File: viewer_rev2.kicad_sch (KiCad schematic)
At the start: 19 parts, among them J1 USB_C_Receptacle_PowerOnly_6P, Q1 DMG3414U, SW1 SW_SPDT, U1 TLC555xD

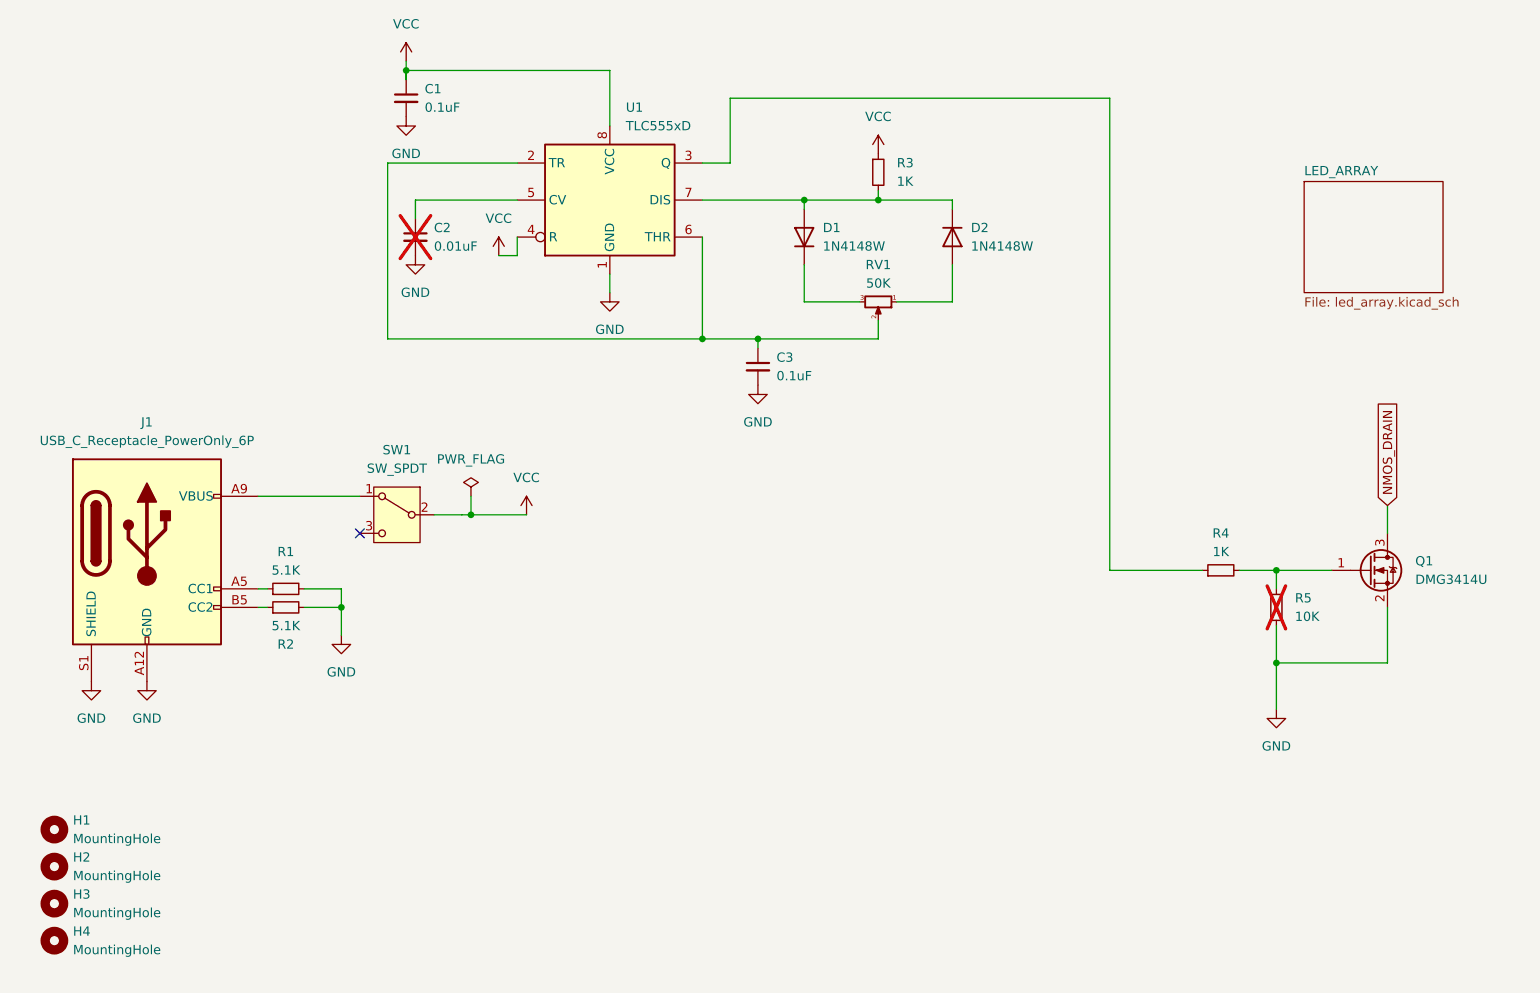
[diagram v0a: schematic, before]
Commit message: update USB-C conn and add JLC PNs
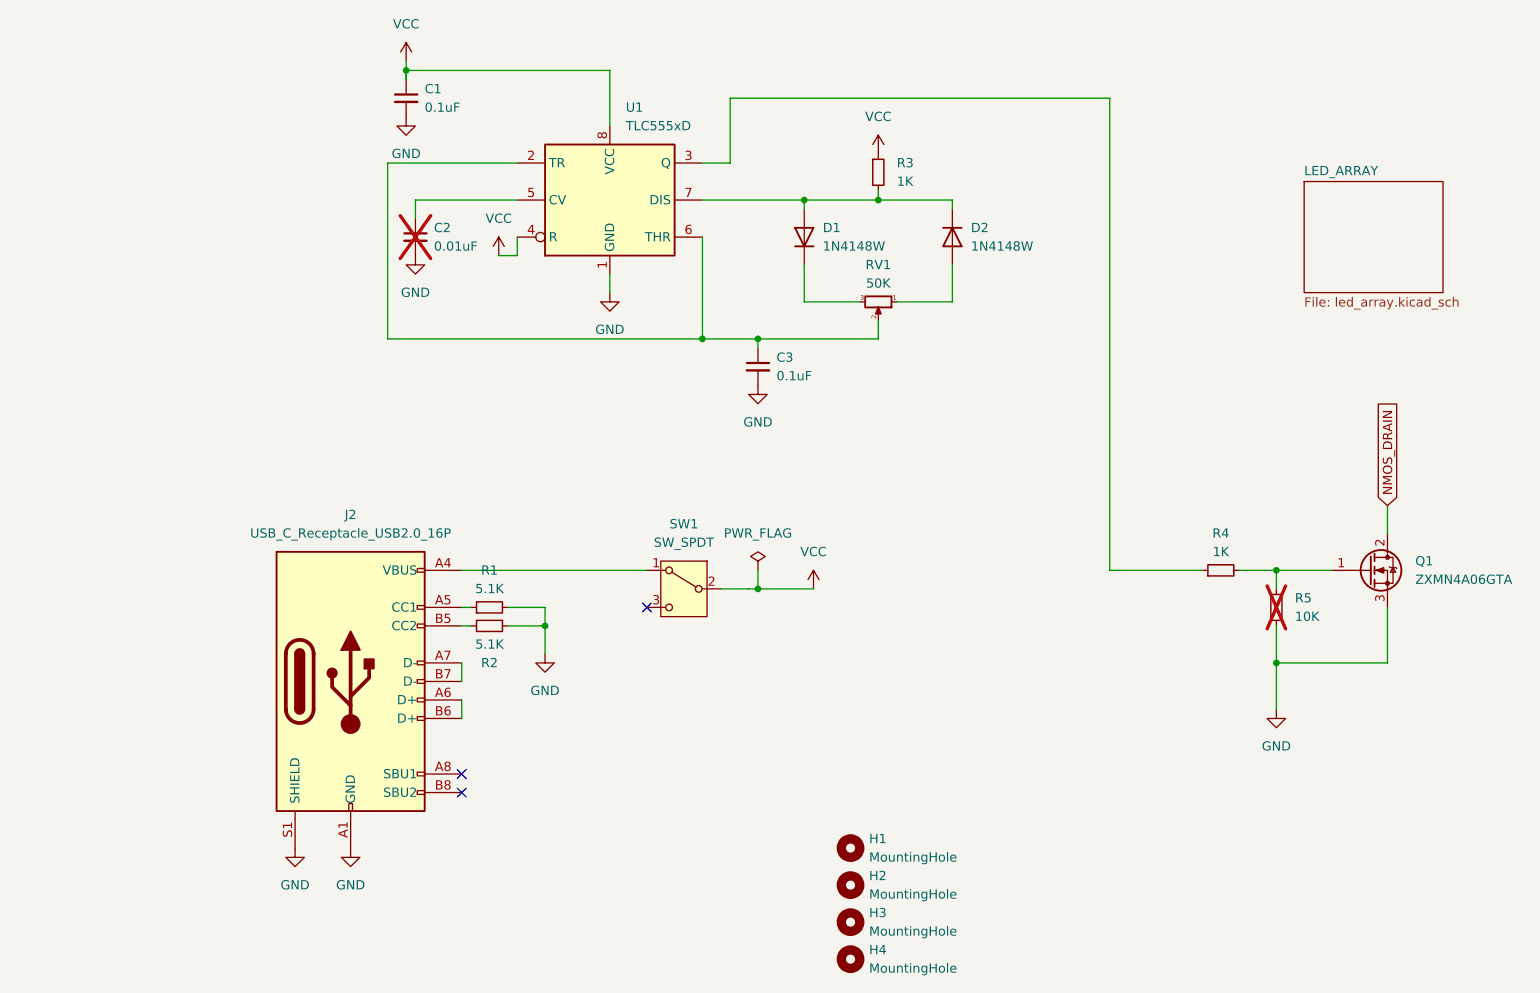
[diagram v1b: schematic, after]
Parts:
- removed J1: USB_C_Receptacle_PowerOnly_6P, Connector_USB:USB_C_Receptacle_GCT_USB4125-xx-x_6P_TopMnt_Horizontal, symbol Connector:USB_C_Receptacle_PowerOnly_6P
- removed Q1: DMG3414U, Package_TO_SOT_SMD:SOT-23, symbol Transistor_FET:DMG3414U
- added J2: USB_C_Receptacle_USB2.0_16P, Connector_USB:USB_C_Receptacle_GCT_USB4105-xx-A_16P_TopMnt_Horizontal, symbol Connector:USB_C_Receptacle_USB2.0_16P
- added Q1: ZXMN4A06GTA, Package_TO_SOT_SMD:SOT-223-3_TabPin2, symbol Device:Q_NMOS_GDS
- C1, C3: JLC (none) -> C14663
- C2: JLC (none) -> C57112
- D1, D2: JLC (none) -> C191428
- R1, R2: JLC (none) -> C23186
- R3, R4: JLC (none) -> C21190
- R5: JLC (none) -> C25804
- RV1: JLC (none) -> C7029921
- SW1: JLC (none) -> C273395
- U1: JLC (none) -> C6986
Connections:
- net GND: now also J2.A1 (GND), J2.A12 (GND), J2.B1 (GND), J2.B12 (GND), J2.S1 (SHIELD), Q1.3 (S)
- net NMOS_DRAIN: now also Q1.2 (D)
- net at R4.2, R5.1: now also Q1.1 (G)
- net at SW1.1 (A): now also J2.A4 (VBUS), J2.A9 (VBUS), J2.B4 (VBUS), J2.B9 (VBUS)
- net at R2.1: now also J2.B5 (CC2)
- net at R1.1: now also J2.A5 (CC1)
- new net: J2.A6 (D+), J2.B6 (D+)
- new net: J2.A7 (D-), J2.B7 (D-)
- no-connect marks 1 -> 3
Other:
- moved on the sheet: H1, H2, H3, H4, R1, R2, SW1

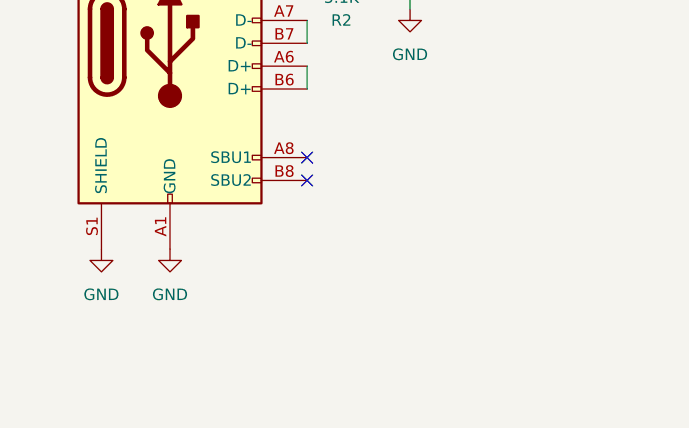
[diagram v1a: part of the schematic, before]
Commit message: Modify clearance setting and change to fit. Other changes to satisfy ERC / DRC
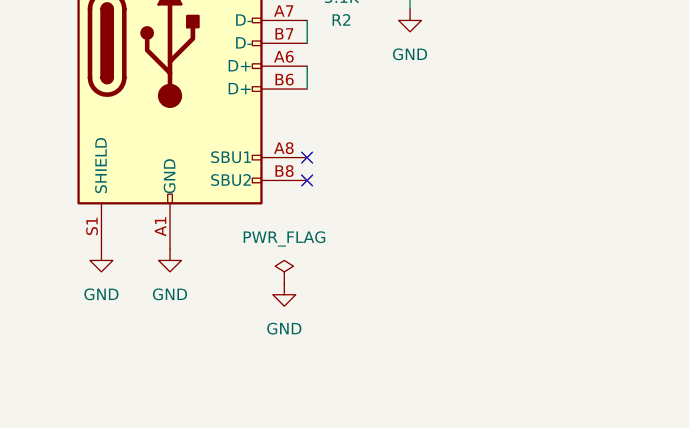
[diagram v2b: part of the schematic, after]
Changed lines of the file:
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@@
+    )
+  )
+  (symbol (lib_id "power:PWR_FLAG") (at 78.74 170.18 0) (unit 1)
+    (in_bom yes) (on_board yes) (dnp no) (fields_autoplaced)
+    (property "Reference" "#FLG02" (at 78.74 168.275 0)
+      (effects (font (size 1.27 1.27)) hide)
+    )
+    (property "Value" "PWR_FLAG" (at 78.74 165.1 0)
+      (effects (font (size 1.27 1.27)))
+    )
+    (property "Footprint" "" (at 78.74 170.18 0)
+      (effects (font (size 1.27 1.27)) hide)
+    )
+    (property "Datasheet" "~" (at 78.74 170.18 0)
+      (effects (font (size 1.27 1.27)) hide)
+    )
+    (pin "1")
+    (instances
+      (project "viewer_rev2"
+        (path "/d62aa8b7-309b-4168-a314-ed1e3433609c"
+          (reference "#FLG02") (unit 1)
+        )
+      )
+    )
+  )
+  (symbol (lib_id "power:GND") (at 78.74 170.18 0) (unit 1)
+    (in_bom yes) (on_board yes) (dnp no) (fields_autoplaced)
+    (property "Reference" "#PWR025" (at 78.74 176.53 0)
+      (effects (font (size 1.27 1.27)) hide)
+    )
+    (property "Value" "GND" (at 78.74 175.26 0)
+      (effects (font (size 1.27 1.27)))
+    )
+    (property "Footprint" "" (at 78.74 170.18 0)
+      (effects (font (size 1.27 1.27)) hide)
+    )
+    (property "Datasheet" "" (at 78.74 170.18 0)
+      (effects (font (size 1.27 1.27)) hide)
+    )
+    (pin "1")
+    (instances
+      (project "viewer_rev2"
+        (path "/d62aa8b7-309b-4168-a314-ed1e3433609c"
+          (reference "#PWR025") (unit 1)
+        )
+      )
     )
   )

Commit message: Add DigiKey and Mouser PNs. Update manf outputs
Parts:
- Q1: Mouser (none) -> 522-ZXMN4A06GTA
- R3, R4: DigiKey 311-1.0KARCT-ND -> (none); Mouser 603-RC0805JR-071KL -> (none)
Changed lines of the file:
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@@
       (effects (font (size 1.27 1.27)) hide)
     )
-    (property "DigiKey" "311-1.0KARCT-ND" (at 138.43 73.66 0)
-      (effects (font (size 1.27 1.27)) hide)
-    )
-    (property "Mouser" "603-RC0805JR-071KL" (at 138.43 73.66 0)
+    (property "DigiKey" "" (at 138.43 73.66 0)
+      (effects (font (size 1.27 1.27)) hide)
+    )
+    (property "Mouser" "" (at 138.43 73.66 0)
       (effects (font (size 1.27 1.27)) hide)
     )
@@
       (effects (font (size 1.27 1.27)) hide)
     )
-    (property "DigiKey" "311-1.0KARCT-ND" (at 185.42 128.27 0)
-      (effects (font (size 1.27 1.27)) hide)
-    )
-    (property "Mouser" "603-RC0805JR-071KL" (at 185.42 128.27 0)
+    (property "DigiKey" "" (at 185.42 128.27 0)
+      (effects (font (size 1.27 1.27)) hide)
+    )
+    (property "Mouser" "" (at 185.42 128.27 0)
       (effects (font (size 1.27 1.27)) hide)
     )
@@
       (effects (font (size 1.27 1.27)) hide)
     )
+    (property "Mouser" "522-ZXMN4A06GTA" (at 205.74 128.27 0)
+      (effects (font (size 1.27 1.27)) hide)
+    )

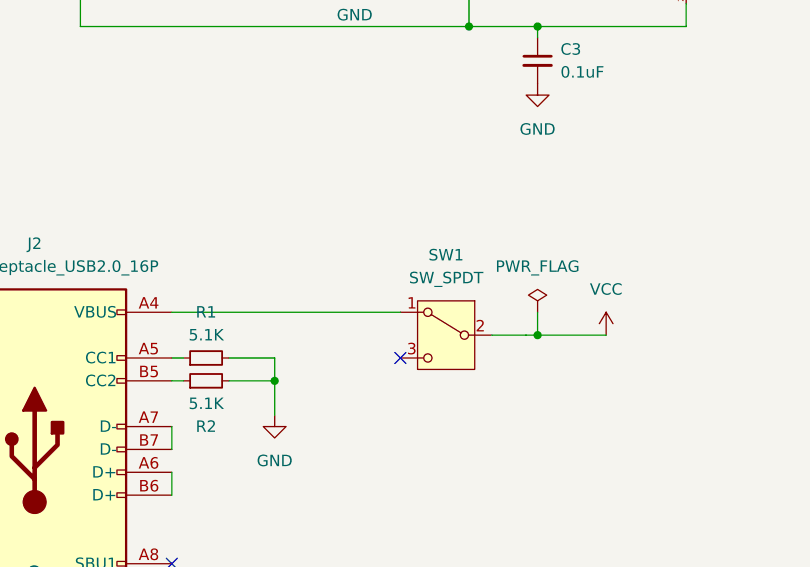
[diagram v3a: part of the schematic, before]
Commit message: part change to higher current switch. Export manf for new PCB and new BOM.
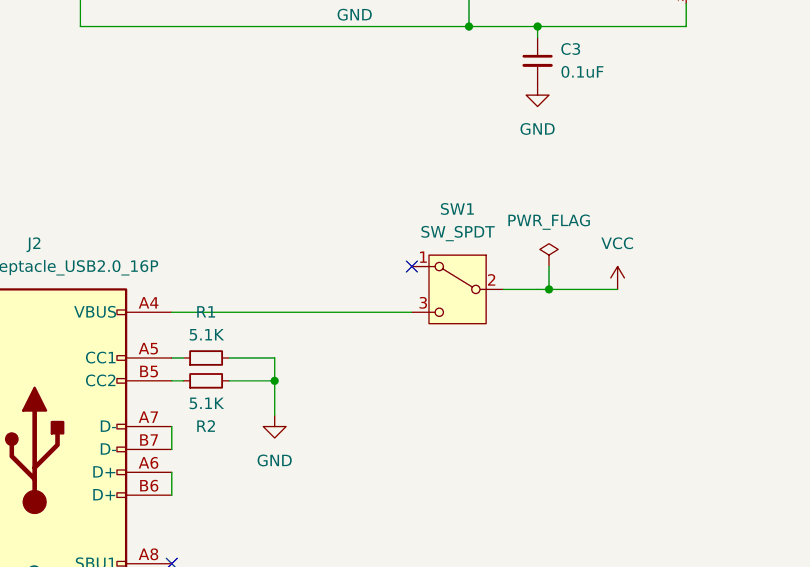
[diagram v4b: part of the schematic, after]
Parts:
- C1, C3: DigiKey 311-1140-1-ND -> (none); Mouser 603-CC805KRX7R9BB104 -> (none)
- C2: DigiKey 311-1136-1-ND -> (none); Mouser 603-CC805KRX7R9BB103 -> (none)
- SW1: footprint Button_Switch_THT:SW_E-Switch_EG1224_SPDT_Angled -> Switch:1101MxSxAxx; DigiKey EG2585-ND -> CKN11550-ND; JLC C273395 -> C2800020; Mouser 612-EG1224 -> 611-1101M2S5AQE2
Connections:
- net at J2.A4 (VBUS), J2.A9 (VBUS), J2.B4 (VBUS)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: now also SW1.3 (C); no longer SW1.1 (A)
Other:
- moved on the sheet: SW1
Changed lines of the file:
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@@
 (kicad_sch (version 20230121) (generator eeschema)
   (paper "A4")
-  (junction (at 121.92 130.81) (diameter 0) (color 0 0 0 0)
+  (junction (at 123.19 125.73) (diameter 0) (color 0 0 0 0)
   )
   (junction (at 128.27 77.47) (diameter 0) (color 0 0 0 0)
@@
   )
   (no_connect (at 81.28 156.21))
-  (no_connect (at 106.68 133.35))
+  (no_connect (at 107.95 123.19))
   (no_connect (at 81.28 158.75))
   (wire (pts (xy 92.71 133.35) (xy 92.71 135.89))
@@
     (stroke (width 0) (type default))
   )
-  (wire (pts (xy 121.92 130.81) (xy 129.54 130.81))
+  (wire (pts (xy 123.19 125.73) (xy 130.81 125.73))
     (stroke (width 0) (type default))
   )
@@
     (stroke (width 0) (type default))
   )
-  (wire (pts (xy 121.92 128.27) (xy 121.92 130.81))
+  (wire (pts (xy 123.19 123.19) (xy 123.19 125.73))
     (stroke (width 0) (type default))
   )
@@
     (stroke (width 0) (type default))
   )
-  (wire (pts (xy 121.92 130.81) (xy 120.65 130.81))
+  (wire (pts (xy 123.19 125.73) (xy 121.92 125.73))
     (stroke (width 0) (type default))
   )
@@
     (stroke (width 0) (type default))
   )
-  (wire (pts (xy 116.84 130.81) (xy 120.65 130.81))
+  (wire (pts (xy 118.11 125.73) (xy 121.92 125.73))
     (stroke (width 0.1524) (type solid))
   )
@@
     (stroke (width 0.1524) (type solid))
   )
-  (wire (pts (xy 81.28 128.27) (xy 106.68 128.27))
+  (wire (pts (xy 81.28 128.27) (xy 107.95 128.27))
     (stroke (width 0) (type default))
   )
@@
     )
   )
-  (symbol (lib_id "Switch:SW_SPDT") (at 111.76 130.81 0) (mirror y) (unit 1)
-    (in_bom yes) (on_board yes) (dnp no) (fields_autoplaced)
-    (property "Reference" "SW1" (at 111.76 121.92 0)
-      (effects (font (size 1.27 1.27)))
-    )
-    (property "Value" "SW_SPDT" (at 111.76 124.46 0)
-      (effects (font (size 1.27 1.27)))
-    )
-    (property "Footprint" "Button_Switch_THT:SW_E-Switch_EG1224_SPDT_Angled" (at 111.76 130.81 0)
-      (effects (font (size 1.27 1.27)) hide)
-    )
-    (property "Datasheet" "~" (at 111.76 138.43 0)
-      (effects (font (size 1.27 1.27)) hide)
-    )
-    (property "DigiKey" "EG2585-ND" (at 111.76 130.81 0)
-      (effects (font (size 1.27 1.27)) hide)
-    )
-    (property "Mouser" "612-EG1224" (at 111.76 130.81 0)
-      (effects (font (size 1.27 1.27)) hide)
-    )
-    (property "JLC" "C273395" (at 111.76 130.81 0)
+  (symbol (lib_id "Switch:SW_SPDT") (at 113.03 125.73 0) (mirror y) (unit 1)
+    (in_bom yes) (on_board yes) (dnp no) (fields_autoplaced)
+    (property "Reference" "SW1" (at 113.03 116.84 0)
+      (effects (font (size 1.27 1.27)))
+    )
+    (property "Value" "SW_SPDT" (at 113.03 119.38 0)
+      (effects (font (size 1.27 1.27)))
+    )
+    (property "Footprint" "Switch:1101MxSxAxx" (at 113.03 125.73 0)
+      (effects (font (size 1.27 1.27)) hide)
+    )
+    (property "Datasheet" "https://www.ckswitches.com/media/1429/1000.pdf" (at 113.03 133.35 0)
+      (effects (font (size 1.27 1.27)) hide)
+    )
+    (property "DigiKey" "CKN11550-ND" (at 113.03 125.73 0)
+      (effects (font (size 1.27 1.27)) hide)
+    )
+    (property "Mouser" "611-1101M2S5AQE2" (at 113.03 125.73 0)
+      (effects (font (size 1.27 1.27)) hide)
+    )
+    (property "JLC" "C2800020" (at 113.03 125.73 0)
       (effects (font (size 1.27 1.27)) hide)
     )
@@
       (effects (font (size 1.27 1.27)) hide)
     )
-    (property "DigiKey" "311-1136-1-ND" (at 74.93 82.55 0)
-      (effects (font (size 1.27 1.27)) hide)
-    )
-    (property "Mouser" "603-CC805KRX7R9BB103" (at 74.93 82.55 0)
+    (property "DigiKey" "" (at 74.93 82.55 0)
+      (effects (font (size 1.27 1.27)) hide)
+    )
+    (property "Mouser" "" (at 74.93 82.55 0)
       (effects (font (size 1.27 1.27)) hide)
     )
@@
       (effects (font (size 1.27 1.27)) hide)
     )
-    (property "DigiKey" "311-1140-1-ND" (at 73.66 63.5 0)
-      (effects (font (size 1.27 1.27)) hide)
-    )
-    (property "Mouser" "603-CC805KRX7R9BB104" (at 73.66 63.5 0)
+    (property "DigiKey" "" (at 73.66 63.5 0)
+      (effects (font (size 1.27 1.27)) hide)
+    )
+    (property "Mouser" "" (at 73.66 63.5 0)
       (effects (font (size 1.27 1.27)) hide)
     )
@@
     )
   )
-  (symbol (lib_id "power:PWR_FLAG") (at 121.92 128.27 0) (unit 1)
-    (in_bom yes) (on_board yes) (dnp no) (fields_autoplaced)
-    (property "Reference" "#FLG01" (at 121.92 126.365 0)
-      (effects (font (size 1.27 1.27)) hide)
-    )
-    (property "Value" "PWR_FLAG" (at 121.92 123.19 0)
-      (effects (font (size 1.27 1.27)))
-    )
-    (property "Footprint" "" (at 121.92 128.27 0)
-      (effects (font (size 1.27 1.27)) hide)
-    )
-    (property "Datasheet" "~" (at 121.92 128.27 0)
+  (symbol (lib_id "power:PWR_FLAG") (at 123.19 123.19 0) (unit 1)
+    (in_bom yes) (on_board yes) (dnp no) (fields_autoplaced)
+    (property "Reference" "#FLG01" (at 123.19 121.285 0)
+      (effects (font (size 1.27 1.27)) hide)
+    )
+    (property "Value" "PWR_FLAG" (at 123.19 118.11 0)
+      (effects (font (size 1.27 1.27)))
+    )
+    (property "Footprint" "" (at 123.19 123.19 0)
+      (effects (font (size 1.27 1.27)) hide)
+    )
+    (property "Datasheet" "~" (at 123.19 123.19 0)
       (effects (font (size 1.27 1.27)) hide)
     )
@@
     )
   )
-  (symbol (lib_id "power:VCC") (at 129.54 130.81 0) (unit 1)
-    (in_bom yes) (on_board yes) (dnp no) (fields_autoplaced)
-    (property "Reference" "#PWR08" (at 129.54 134.62 0)
-      (effects (font (size 1.27 1.27)) hide)
-    )
-    (property "Value" "VCC" (at 129.54 125.73 0)
-      (effects (font (size 1.27 1.27)))
-    )
-    (property "Footprint" "" (at 129.54 130.81 0)
-      (effects (font (size 1.27 1.27)) hide)
-    )
-    (property "Datasheet" "" (at 129.54 130.81 0)
+  (symbol (lib_id "power:VCC") (at 130.81 125.73 0) (unit 1)
+    (in_bom yes) (on_board yes) (dnp no) (fields_autoplaced)
+    (property "Reference" "#PWR08" (at 130.81 129.54 0)
+      (effects (font (size 1.27 1.27)) hide)
+    )
+    (property "Value" "VCC" (at 130.81 120.65 0)
+      (effects (font (size 1.27 1.27)))
+    )
+    (property "Footprint" "" (at 130.81 125.73 0)
+      (effects (font (size 1.27 1.27)) hide)
+    )
+    (property "Datasheet" "" (at 130.81 125.73 0)
       (effects (font (size 1.27 1.27)) hide)
     )
@@
       (effects (font (size 1.27 1.27)) hide)
     )
-    (property "DigiKey" "311-1140-1-ND" (at 121.92 100.33 0)
-      (effects (font (size 1.27 1.27)) hide)
-    )
-    (property "Mouser" "603-CC805KRX7R9BB104" (at 121.92 100.33 0)
-      (effects (font (size 1.27 1.27)) hide)
-    )
+    (property "DigiKey" "" (at 121.92 100.33 0)
+      (effects (font (size 1.27 1.27)) hide)
+    )
+    (property "Mouser" "" (at 121.92 100.33 0)
+      (effects (font (size 1.27 1.27)) hide)
+    )
